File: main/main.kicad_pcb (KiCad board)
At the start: 4 copper layers, 72.5 x 60 mm, 35 parts, among them J1 Conn_01x10_Female, J2 USB_B, J3 AVR-ISP-6, J4 Micro_SD_Card, Q1 2N7002, Q2 BSS84, SW1 Reset, U1 ATmega1284P-PU, U2 AMS1117, U3 MCP2221A-I_SL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

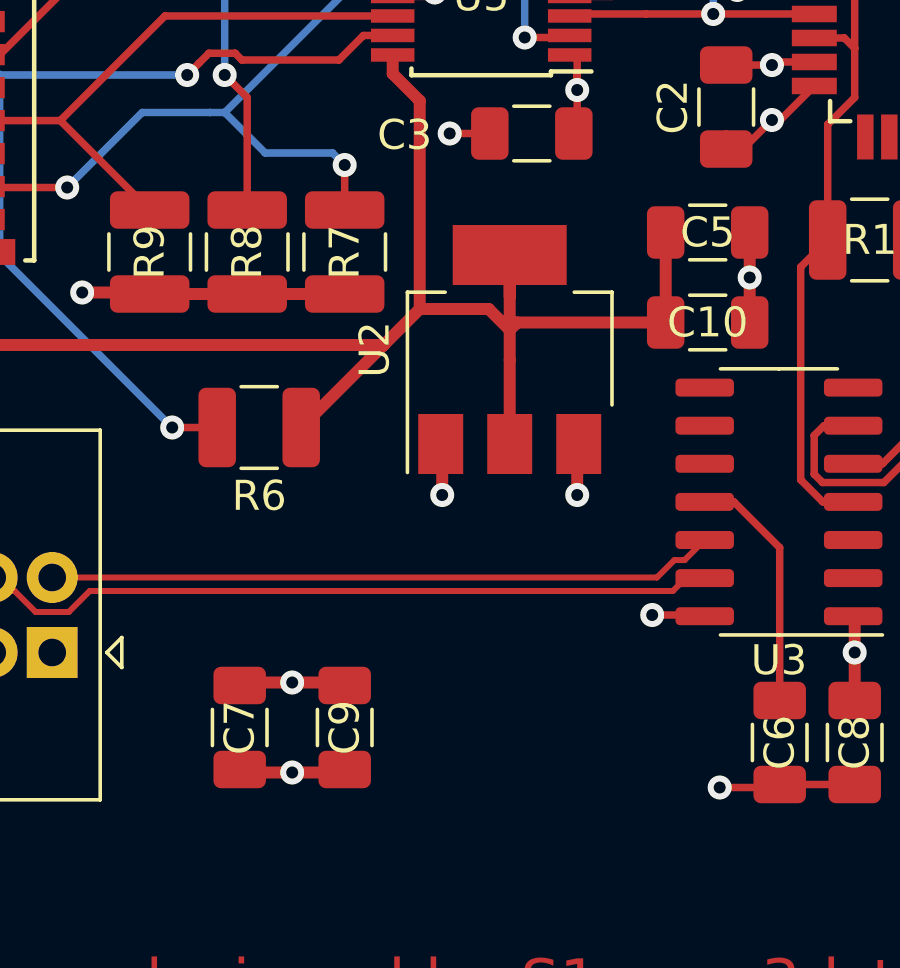
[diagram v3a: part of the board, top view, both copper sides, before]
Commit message: fixed bulking caps
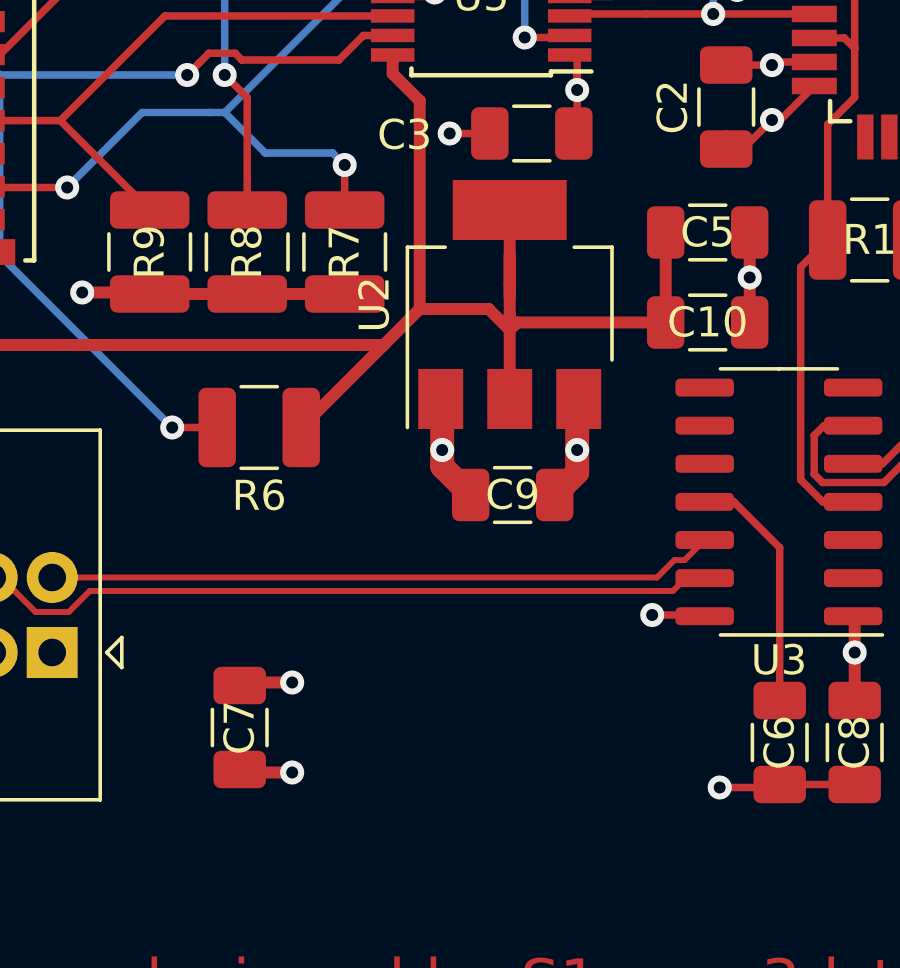
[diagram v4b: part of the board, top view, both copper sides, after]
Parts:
- C7, C9: value 1u -> 10u
- moved C9 9.56 mm to (89.8, 115.5), turned to 180 degrees
- moved U2 1.50 mm to (89.8, 109.2)
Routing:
- net GND: track 50.1 -> 51.9 mm
- net +5V: track 24.7 -> 26.5 mm
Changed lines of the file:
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@@
     (thickness 1.6)
     (drawings 22)
-    (tracks 379)
+    (tracks 383)
     (zones 0)
     (modules 35)
@@
   )
   (setup
-    (last_trace_width 0.4)
-    (user_trace_width 0.25)
+    (last_trace_width 0.8)
     (user_trace_width 0.4)
+    (user_trace_width 0.8)
     (trace_clearance 0.2)
     (zone_clearance 0.508)
@@
   )
   (module Capacitor_SMD:C_1206_3216Metric (layer F.Cu)
-    (at 84.25 123.25 270)
+    (at 89.85 115.5 180)
     (descr "Capacitor SMD 1206 (3216 Metric), square (rectangular) end terminal, IPC_7351 nominal, (Body size source: http://www.tortai-tech.com/upload/download/2011102023233369053.pdf), generated with kicad-footprint-generator")
     (tags capacitor)
     (attr smd)
-    (fp_text reference C9 (at 0 0 90) (layer F.SilkS)
-      (effects (font (size 1 1) (thickness 0.15)))
-    )
-    (fp_text value 1u (at 0 1.82 90) (layer F.Fab)
-      (effects (font (size 1 1) (thickness 0.15)))
-    )
-    (fp_text user %R (at 0 0 90) (layer F.Fab)
+    (fp_text reference C9 (at 0 0) (layer F.SilkS)
+      (effects (font (size 1 1) (thickness 0.15)))
+    )
+    (fp_text value 10u (at 0 1.82) (layer F.Fab)
+      (effects (font (size 1 1) (thickness 0.15)))
+    )
+    (fp_text user %R (at 0 0) (layer F.Fab)
       (effects (font (size 0.8 0.8) (thickness 0.12)))
     )
@@
     (fp_line (start -1.6 -0.8) (end 1.6 -0.8) (layer F.Fab) (width 0.1))
     (fp_line (start -1.6 0.8) (end -1.6 -0.8) (layer F.Fab) (width 0.1))
-    (pad 2 smd roundrect (at 1.4 0 270) (size 1.25 1.75) (layers F.Cu F.Paste F.Mask) (roundrect_rratio 0.2)
-      (net 1 GND))
-    (pad 1 smd roundrect (at -1.4 0 270) (size 1.25 1.75) (layers F.Cu F.Paste F.Mask) (roundrect_rratio 0.2)
+    (pad 2 smd roundrect (at 1.4 0 180) (size 1.25 1.75) (layers F.Cu F.Paste F.Mask) (roundrect_rratio 0.2)
+      (net 1 GND))
+    (pad 1 smd roundrect (at -1.4 0 180) (size 1.25 1.75) (layers F.Cu F.Paste F.Mask) (roundrect_rratio 0.2)
       (net 2 +5V))
     (model ${KISYS3DMOD}/Capacitor_SMD.3dshapes/C_1206_3216Metric.wrl
@@
   )
   (module Package_TO_SOT_SMD:SOT-223-3_TabPin2 (layer F.Cu)
-    (at 89.75 110.65 90)
+    (at 89.75 109.15 90)
     (descr "module CMS SOT223 4 pins")
     (tags "CMS SOT")
@@
       (effects (font (size 1 1) (thickness 0.15)))
     )
-    (fp_text value 1u (at 0 1.82 90) (layer F.Fab)
+    (fp_text value 10u (at 0 1.82 90) (layer F.Fab)
       (effects (font (size 1 1) (thickness 0.15)))
     )
@@
   (via (at 114 87.75) (size 0.8) (drill 0.4) (layers F.Cu B.Cu) (net 1))
   (via (at 96.75 125.25) (size 0.8) (drill 0.4) (layers F.Cu B.Cu) (net 1))
-  (via (at 87.5 115.5) (size 0.8) (drill 0.4) (layers F.Cu B.Cu) (net 1))
+  (via (at 87.5 114) (size 0.8) (drill 0.4) (layers F.Cu B.Cu) (net 1))
   (via (at 97.75 108.25) (size 0.8) (drill 0.4) (layers F.Cu B.Cu) (net 1))
   (via (at 71 104) (size 0.8) (drill 0.4) (layers F.Cu B.Cu) (net 1))
@@
   (segment (start 61 96.75) (end 59.988101 96.75) (width 0.4) (layer F.Cu) (net 1))
   (segment (start 87.5 113.85) (end 87.45 113.8) (width 0.4) (layer F.Cu) (net 1))
-  (segment (start 87.5 115.5) (end 87.5 113.85) (width 0.4) (layer F.Cu) (net 1))
+  (segment (start 87.5 114.15) (end 87.5 112.5) (width 0.4) (layer F.Cu) (net 1))
   (segment (start 98.65 125.25) (end 98.75 125.15) (width 0.25) (layer F.Cu) (net 1))
   (segment (start 96.75 125.25) (end 98.65 125.25) (width 0.25) (layer F.Cu) (net 1))
@@
   (segment (start 111.25 87.75) (end 114 87.75) (width 0.25) (layer F.Cu) (net 1))
   (segment (start 117 87.75) (end 114 87.75) (width 0.25) (layer F.Cu) (net 1))
-  (segment (start 84.15 124.75) (end 84.25 124.65) (width 0.4) (layer F.Cu) (net 1))
-  (segment (start 82.5 124.75) (end 84.15 124.75) (width 0.4) (layer F.Cu) (net 1))
   (segment (start 80.85 124.75) (end 80.75 124.65) (width 0.4) (layer F.Cu) (net 1))
   (segment (start 82.5 124.75) (end 80.85 124.75) (width 0.4) (layer F.Cu) (net 1))
   (segment (start 97.75 108.25) (end 97.75 106.75) (width 0.4) (layer F.Cu) (net 1))
   (segment (start 97.75 108.25) (end 97.75 109.75) (width 0.4) (layer F.Cu) (net 1))
+  (segment (start 87.5 112.35) (end 87.45 112.3) (width 0.8) (layer F.Cu) (net 1))
+  (segment (start 87.5 114) (end 87.5 112.35) (width 0.8) (layer F.Cu) (net 1))
+  (segment (start 87.5 114.55) (end 88.45 115.5) (width 0.8) (layer F.Cu) (net 1))
+  (segment (start 87.5 114) (end 87.5 114.55) (width 0.8) (layer F.Cu) (net 1))
   (via (at 82.5 121.75) (size 0.8) (drill 0.4) (layers F.Cu B.Cu) (net 2))
   (via (at 103.25 109.25) (size 0.8) (drill 0.4) (layers F.Cu B.Cu) (net 2))
-  (via (at 92 115.5) (size 0.8) (drill 0.4) (layers F.Cu B.Cu) (net 2))
+  (via (at 92 114) (size 0.8) (drill 0.4) (layers F.Cu B.Cu) (net 2))
   (via (at 99.5 85.75) (size 0.8) (drill 0.4) (layers F.Cu B.Cu) (net 2))
   (via (at 80.75 96) (size 0.8) (drill 0.4) (layers F.Cu B.Cu) (net 2))
@@
   (segment (start 99.5 85.75) (end 98 85.75) (width 0.25) (layer F.Cu) (net 2))
   (segment (start 92 113.85) (end 92.05 113.8) (width 0.4) (layer F.Cu) (net 2))
-  (segment (start 92 115.5) (end 92 113.85) (width 0.4) (layer F.Cu) (net 2))
+  (segment (start 92 114.15) (end 92 112.5) (width 0.4) (layer F.Cu) (net 2))
   (segment (start 101.25 119.59) (end 101.2 119.54) (width 0.4) (layer F.Cu) (net 2))
   (segment (start 101.25 122.35) (end 101.25 120.75) (width 0.4) (layer F.Cu) (net 2))
@@
   (segment (start 103.25 107.1) (end 103.15 107) (width 0.25) (layer F.Cu) (net 2))
   (segment (start 103.25 109.25) (end 103.25 107.1) (width 0.25) (layer F.Cu) (net 2))
-  (segment (start 84.15 121.75) (end 84.25 121.85) (width 0.4) (layer F.Cu) (net 2))
-  (segment (start 82.5 121.75) (end 84.15 121.75) (width 0.4) (layer F.Cu) (net 2))
   (segment (start 80.85 121.75) (end 80.75 121.85) (width 0.4) (layer F.Cu) (net 2))
   (segment (start 82.5 121.75) (end 80.85 121.75) (width 0.4) (layer F.Cu) (net 2))
+  (segment (start 92 114.75) (end 91.25 115.5) (width 0.8) (layer F.Cu) (net 2))
+  (segment (start 92 114) (end 92 114.75) (width 0.8) (layer F.Cu) (net 2))
+  (segment (start 92 112.35) (end 92.05 112.3) (width 0.8) (layer F.Cu) (net 2))
+  (segment (start 92 114) (end 92 112.35) (width 0.8) (layer F.Cu) (net 2))
   (segment (start 71.427 101.920001) (end 70.0761 103.270901) (width 0.4) (layer F.Cu) (net 3))
   (segment (start 85.55 110.5) (end 82.8 113.25) (width 0.4) (layer F.Cu) (net 3))
@@
   (segment (start 86.75 102.357) (end 85.85 101.457) (width 0.4) (layer F.Cu) (net 3))
   (segment (start 86.75 109.3) (end 86.75 102.357) (width 0.4) (layer F.Cu) (net 3))
-  (segment (start 89.75 113.8) (end 89.75 111) (width 0.4) (layer F.Cu) (net 3))
+  (segment (start 89.75 112.3) (end 89.75 109.5) (width 0.4) (layer F.Cu) (net 3))
   (segment (start 86.75 109.3) (end 89.05 109.3) (width 0.4) (layer F.Cu) (net 3))
-  (segment (start 89.75 111) (end 89.75 110) (width 0.4) (layer F.Cu) (net 3))
+  (segment (start 89.75 109.5) (end 89.75 108.5) (width 0.4) (layer F.Cu) (net 3))
   (segment (start 89.05 109.3) (end 89.75 110) (width 0.4) (layer F.Cu) (net 3))
-  (segment (start 89.75 110) (end 89.75 107.5) (width 0.4) (layer F.Cu) (net 3))
+  (segment (start 89.75 108.5) (end 89.75 106) (width 0.4) (layer F.Cu) (net 3))
   (segment (start 70.0761 94.816099) (end 70.0761 103.270901) (width 0.4) (layer F.Cu) (net 3))
   (segment (start 85.425 93) (end 72 93) (width 0.4) (layer F.Cu) (net 3))
